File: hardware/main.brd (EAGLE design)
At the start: 87.6 x 68.1 mm, 60 parts, among them CON1 WIRE2BOARD_10POS, CON2 WIRE2BOARD_10POS, U1 SN74LVC4245A_DW_24, U2 Value, U3 SN74ABT541B_DW_20, U4 SN74LVC1G04_DBV_5, U5 SN74LVC4245A_DW_24, U6 Value, U7 TXB0101_DBV_6, U8 8BIT-DIP-SWITCH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

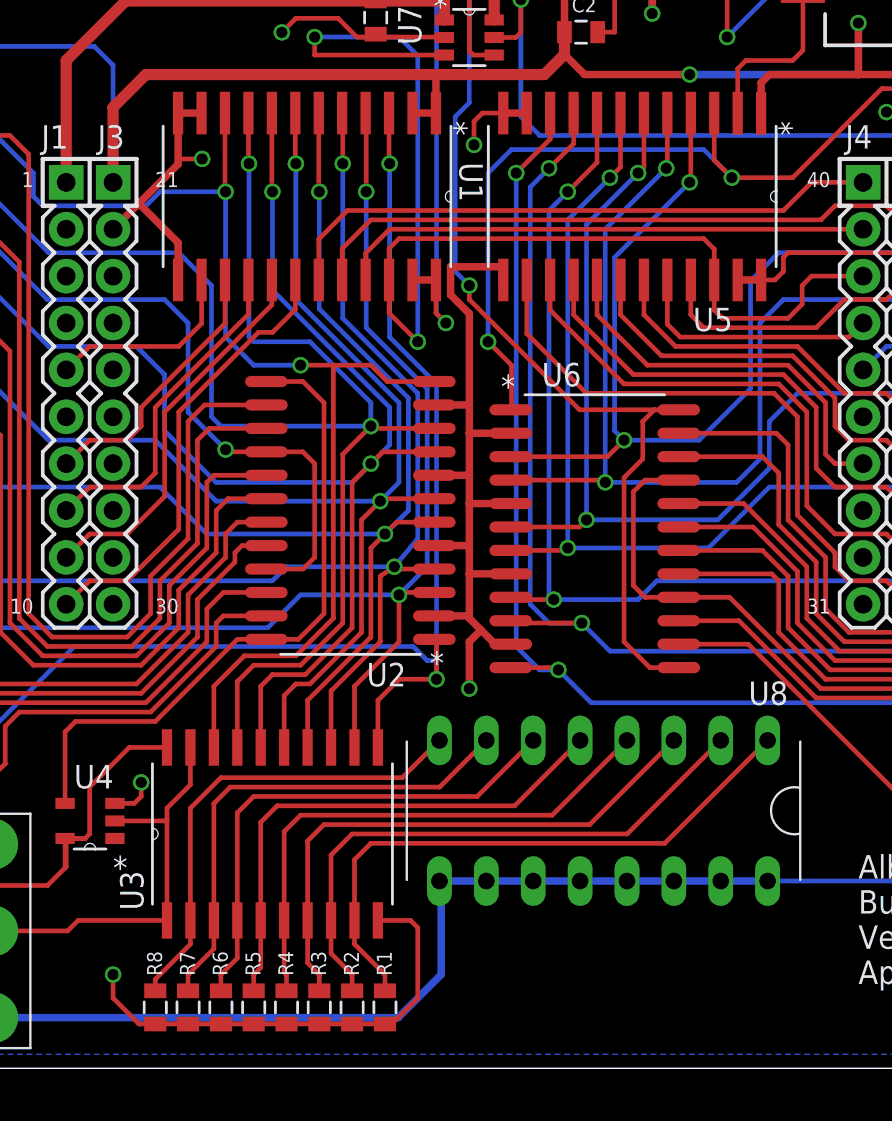
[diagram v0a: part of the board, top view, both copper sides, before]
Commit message: Cleaned up board. Cleaned up schematic. No structural or electrical changes
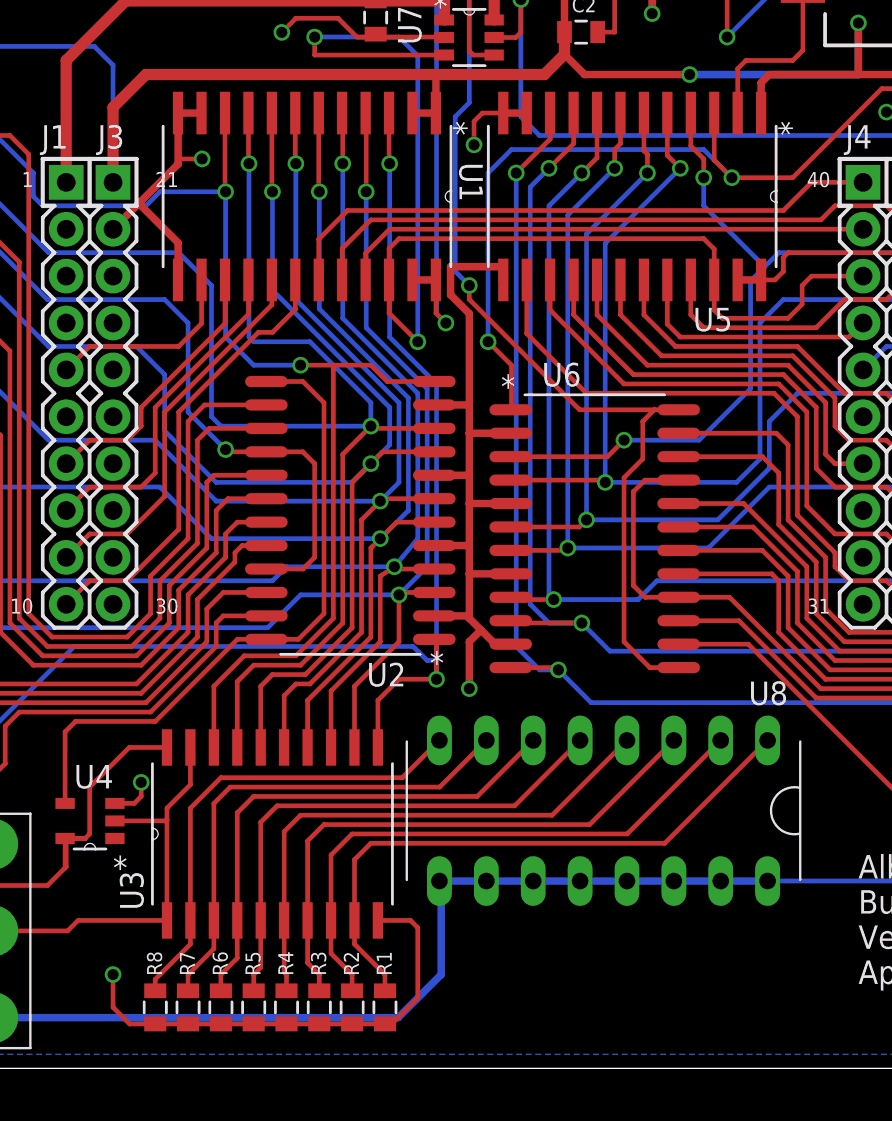
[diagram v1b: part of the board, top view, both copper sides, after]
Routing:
- net LEDOUT2: track 57.2 -> 47.5 mm
- net LEDOUT3: track 58.4 -> 59.0 mm
